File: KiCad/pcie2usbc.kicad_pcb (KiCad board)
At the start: 4 copper layers, 35.3 x 24 mm, 126 parts, among them J2 USB-C-MLX, J3 Bus_PCI_Express_x4, J4 Conn_02x05_Top_Bottom, J5 USB-C-MLX

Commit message: WiP layout
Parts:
- removed the C1 at (194.6, 94.7)
- removed the C10 at (194.6, 97.5)
- removed the C10 at (145.9, 97.8)
- removed the C11 at (194.6, 100.3)
- removed the C11 at (145.9, 96.0)
- removed the C12 at (194.6, 103.1)
- removed the C12 at (145.9, 103.0)
- removed the C13 at (194.6, 105.9)
- removed the C13 at (145.9, 101.3)
- removed the C16 at (223.7, 94.7)
- removed the C16 at (159.2, 104.0)
- removed the C17 at (223.0, 108.3)
- removed the C17 at (160.2, 104.0)
- removed the C2 at (158.2, 104.0)
- removed the C3 at (162.4, 104.0)
- removed the C4 at (193.9, 112.5)
- removed the C4 at (161.4, 104.0)
- removed the C5 at (193.9, 114.6)
- removed the C5 at (156.9, 104.0)
- removed the C6 at (193.9, 116.7)
- removed the C6 at (157.9, 104.0)
- removed the C7 at (162.2, 104.0)
- removed the C8 at (161.2, 104.0)
- removed the C9 at (196.9, 112.5)
- removed the C9 at (151.9, 96.0)
- removed the J2 at (185.4, 98.5)
- removed the R10 at (199.8, 77.9)
- removed the R10 at (145.9, 99.5)
- removed the R2 at (198.9, 97.5)
- removed the R2 at (136.9, 106.5)
- removed R21: 0, pcie2usbc:R0603
- removed R22: 100k, pcie2usbc:R0603
- removed the R3 at (198.9, 100.3)
- removed the R3 at (151.9, 103.0)
- removed the R4 at (198.9, 103.1)
- removed the R4 at (151.9, 97.8)
- removed the R5 at (198.9, 105.9)
- removed the R5 at (151.9, 101.3)
- removed the R6 at (203.3, 94.7)
- removed the R6 at (151.9, 99.5)
- removed the R7 at (203.3, 97.5)
- removed the R7 at (134.7, 106.5)
- removed the R8 at (203.3, 100.3)
- removed the R8 at (132.4, 106.5)
- removed RST0, UNK12V0, UNK3V3: , pcie2usbc:SML0805
- removed TP1, TP2, TP21, TP3, TP4, TP5, TP6, TP7, TP8, TP9: TPB0,635, pcie2usbc:B0,635
- removed the TP13 at (180.7, 113.6)
- removed the TP13 at (164.7, 105.8)
- removed the TP16 at (159.7, 95.0)
- removed the TP16 at (187.6, 78.5)
- removed the TP19 at (191.6, 78.5)
- removed TP20, TP21, TP22, TP23, TP24, TP31, TP32, TP33, TP34, TP35, TP36, TP37, TP38: TestPoint, TestPoint:TestPoint_Pad_D2.0mm
- removed TP30: TPTP38X20, pcie2usbc:TP38X20
- removed UNK12V1, UNK12V2, UNK3V1, UNK3V2: LEDSML0805, pcie2usbc:SML0805
- added +12V1: LEDSML0805, pcie2usbc:SML0805, F.Cu at (149.2, 79.5)
- added +12V2: LEDSML0805, pcie2usbc:SML0805, F.Cu at (184.4, 78.9)
- added +3V1: LEDSML0805, pcie2usbc:SML0805, F.Cu at (146.6, 79.5)
- added +3V2: LEDSML0805, pcie2usbc:SML0805, F.Cu at (187.0, 78.7)
- added C10: 100n, pcie2usbc:C0402, B.Cu at (161.6, 89.9)
- added C11: 100n, pcie2usbc:C0402, B.Cu at (158.3, 86.0)
- added C12: 1u, pcie2usbc:C0603K, F.Cu at (145.3, 104.0)
- added C13: 100n, pcie2usbc:C0603K, F.Cu at (147.2, 104.0)
- added C16: 100n, pcie2usbc:C0603K, F.Cu at (169.0, 78.7)
- added C17: 100n, pcie2usbc:C0402, F.Cu at (180.9, 90.9)
- added C4: 100n, pcie2usbc:C0402, B.Cu at (153.3, 90.0)
- added C5: 100n, pcie2usbc:C0402, B.Cu at (160.2, 89.8)
- added C6: 100n, pcie2usbc:C0402, B.Cu at (157.1, 86.0)
- added C9: 100n, pcie2usbc:C0402, B.Cu at (154.6, 90.0)
- added R10: 0, Resistor_SMD:R_0402_1005Metric_Pad0.72x0.64mm_HandSolder, B.Cu at (145.3, 87.1)
- added R2: 0, Resistor_SMD:R_0402_1005Metric_Pad0.72x0.64mm_HandSolder, B.Cu at (172.2, 98.4)
- added R3: 2.2k, Resistor_SMD:R_0402_1005Metric_Pad0.72x0.64mm_HandSolder, F.Cu at (143.6, 83.1)
- added R4: 10k, Resistor_SMD:R_0402_1005Metric_Pad0.72x0.64mm_HandSolder, F.Cu at (149.1, 82.9)
- added R5: 2.2k, Resistor_SMD:R_0402_1005Metric_Pad0.72x0.64mm_HandSolder, F.Cu at (146.5, 83.0)
- added R7: 0, Resistor_SMD:R_0402_1005Metric_Pad0.72x0.64mm_HandSolder, B.Cu at (148.4, 87.1)
- added R8: 0, Resistor_SMD:R_0402_1005Metric_Pad0.72x0.64mm_HandSolder, B.Cu at (148.5, 86.0)
- added TP13: TestPoint, TestPoint:TestPoint_Pad_1.0x1.0mm, B.Cu at (141.7, 88.3)
- added TP15: TestPoint, TestPoint:TestPoint_Pad_1.0x1.0mm, F.Cu at (136.8, 87.3)
- added TP16: TestPoint, TestPoint:TestPoint_Pad_1.0x1.0mm, F.Cu at (137.0, 80.9)
- C1: footprint pcie2usbc:C0402 -> pcie2usbc:C0603K; moved to B.Cu
- C14: value 100n -> 1u; footprint pcie2usbc:C0402 -> pcie2usbc:C0603K
- C15: footprint pcie2usbc:C0402 -> pcie2usbc:C0603K
- C2, C27, C28, C29, C3, C30, C7, C8: moved to B.Cu
- J3: renamed from J2; footprint pcie2usbc:MOLEX_105450-0101 -> Connector_USB:USB_C_Receptacle_CNCTech_C-ARA1-AK51X
- J4: renamed from J5; footprint pcie2usbc:MOLEX_105450-0101 -> Connector_USB:USB_C_Receptacle_CNCTech_C-ARA1-AK51X
- R1: footprint pcie2usbc:R0603 -> Resistor_SMD:R_0402_1005Metric_Pad0.72x0.64mm_HandSolder; moved to B.Cu
- R11, R20: value 0 -> 100k; footprint pcie2usbc:R0603 -> Resistor_SMD:R_0402_1005Metric_Pad0.72x0.64mm_HandSolder
- R12: value 0 -> 2.2k; footprint pcie2usbc:R0603 -> Resistor_SMD:R_0402_1005Metric_Pad0.72x0.64mm_HandSolder
- R13: value 2.2k -> 10k; footprint pcie2usbc:R0603 -> Resistor_SMD:R_0402_1005Metric_Pad0.72x0.64mm_HandSolder
- R14: value 10k -> 2.2k; footprint pcie2usbc:R0603 -> Resistor_SMD:R_0402_1005Metric_Pad0.72x0.64mm_HandSolder
- R15: value 2.2k -> 0; footprint pcie2usbc:R0603 -> Resistor_SMD:R_0402_1005Metric_Pad0.72x0.64mm_HandSolder; moved to B.Cu
- R16: footprint pcie2usbc:R0603 -> Resistor_SMD:R_0402_1005Metric_Pad0.72x0.64mm_HandSolder; moved to F.Cu
- R17, R18, R19: footprint pcie2usbc:R0603 -> Resistor_SMD:R_0402_1005Metric_Pad0.72x0.64mm_HandSolder
- R6: renamed from R1; value 100k -> 0; footprint pcie2usbc:R0603 -> Resistor_SMD:R_0402_1005Metric_Pad0.72x0.64mm_HandSolder
- R9: value 100k -> 0; footprint pcie2usbc:R0603 -> Resistor_SMD:R_0402_1005Metric_Pad0.72x0.64mm_HandSolder; moved to B.Cu
- TP10: value TPTP38X20 -> TestPoint; footprint pcie2usbc:TP38X20 -> TestPoint:TestPoint_Pad_1.0x1.0mm
- TP11, TP12: value TPB0,635 -> TestPoint; footprint pcie2usbc:B0,635 -> TestPoint:TestPoint_Pad_1.0x1.0mm; moved to B.Cu
- TP14: renamed from TP10; footprint pcie2usbc:TP38X20 -> TestPoint:TestPoint_Pad_D1.5mm
- TP17, TP18: footprint TestPoint:TestPoint_Pad_D2.0mm -> TestPoint:TestPoint_Pad_1.0x1.0mm
- TP19: renamed from TP29; footprint pcie2usbc:TP38X20 -> TestPoint:TestPoint_Pad_D1.5mm
- moved C30 88.6 mm to (135.2, 102.3), turned to 180 degrees
- moved C29 88.5 mm to (135.2, 104.3), turned to 180 degrees
- moved R15 84.9 mm to (143.6, 91.5)
- moved C27 78.7 mm to (145.3, 104.0), turned to 90 degrees
- moved C28 76.6 mm to (147.2, 104.0), turned to 90 degrees
- moved R20 66.1 mm to (169.5, 77.1)
- moved C26 65.1 mm to (165.9, 91.9), turned to -90 degrees
- moved RST1 64.3 mm to (143.7, 79.5), turned to 90 degrees
- moved C21 63.6 mm to (164.5, 91.8), turned to -90 degrees
- moved C15 63.4 mm to (135.2, 102.3), turned to 180 degrees
- moved C14 62.6 mm to (135.2, 104.2), turned to 180 degrees
- moved R9 60.4 mm to (145.3, 86.0), turned to 180 degrees
- moved C25 59.3 mm to (171.3, 92.0), turned to -90 degrees
- moved R17 58.6 mm to (171.7, 86.8)
- moved C20 57.6 mm to (170.1, 92.0), turned to -90 degrees
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- renumbered J3 to J1, J4 to J2
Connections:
- C1 pad 1: RX1_P -> Net-(C1-Pad1)
- C1 pad 2: PER0_P -> GND
- C14 pad 1: /USB-C Lane1+2/TX2_N -> +3V3
- C14 pad 2: /PET1_N -> GND
- C15 pad 1: /USB-C Lane1+2/D_N -> +3V3
- C15 pad 2: /REFCLK_N -> GND
- J3 pad A10: RX2_N -> /USB-C Lane1+2/RX2_N
- J3 pad A11: RX2_P -> /USB-C Lane1+2/RX2_P
- J3 pad A2: TX1_P -> /USB-C Lane1+2/TX1_P
- J3 pad A3: TX1_N -> /USB-C Lane1+2/TX1_N
- J3 pad A4: VBUS -> /USB-C Lane1+2/VBUS
- J3 pad A5: CC1 -> /USB-C Lane1+2/CC1
- J3 pad A6: D_P -> /USB-C Lane1+2/D_P
- J3 pad A7: D_N -> /USB-C Lane1+2/D_N
- J3 pad A8: SBU1 -> /USB-C Lane1+2/SBU1
- J3 pad A9: VBUS -> /USB-C Lane1+2/VBUS
- J3 pad B10: RX1_N -> /USB-C Lane1+2/RX1_N
- J3 pad B11: RX1_P -> /USB-C Lane1+2/RX1_P
- J3 pad B2: TX2_P -> /USB-C Lane1+2/TX2_P
- J3 pad B3: TX2_N -> /USB-C Lane1+2/TX2_N
- J3 pad B4: VBUS -> /USB-C Lane1+2/VBUS
- J3 pad B5: CC2 -> /USB-C Lane1+2/CC2
- J3 pad B6: D_P -> /USB-C Lane1+2/D_P
- J3 pad B7: D_N -> /USB-C Lane1+2/D_N
- J3 pad B8: SBU2 -> /USB-C Lane1+2/SBU2
- J3 pad B9: VBUS -> /USB-C Lane1+2/VBUS
- J3 pad S1: USB_SHLD1 -> Net-(C1-Pad1)
- R1 pad 1: /VBUS_H -> /PRSNT_SEL
- R1 pad 2: /USB-C Lane1+2/VBUS -> /PRSNT2
- R11 pad 1: PRSNT_SEL -> GND
- R11 pad 2: PRSNT2_N -> Net-(C1-Pad1)
- R12 pad 1: /PRSNT1 -> /PERST_N
- R12 pad 2: /PRSNT_SEL -> Net-(R12-Pad2)
- R13 pad 1: /PERST_N -> GND
- R13 pad 2: Net-(R13-Pad2) -> Net-(+12V2-PadC)
- R15 pad 1: GND -> /VBUS_H
- R15 pad 2: Net-(R15-Pad2) -> /USB-C Lane3+4/VBUS
- R16 pad 1: PRSNT1_N -> /PRSNT2_N
- R16 pad 2: PRSNT_SEL -> /USB-C Lane3+4/SBU1
- R17 pad 1: /VBUS_H -> /PRSNT1_N
- R17 pad 2: /USB-C Lane3+4/VBUS -> /USB-C Lane3+4/SBU2
- R18 pad 1: /PRSNT2_N -> /PERST_N
- R18 pad 2: /USB-C Lane3+4/SBU1 -> /USB-C Lane3+4/CC1
- R19 pad 1: /PRSNT1_N -> /USB-C Lane3+4/CC2
- R19 pad 2: /USB-C Lane3+4/SBU2 -> /PERST_N
- R20 pad 1: /PERST_N -> GND
- R20 pad 2: /USB-C Lane3+4/CC1 -> Net-(C16-Pad1)
- R6 pad 1: GND -> /VBUS_H
- R6 pad 2: USB_SHLD1 -> /USB-C Lane1+2/VBUS
- R9 pad 1: GND -> /PERST_N
- R9 pad 2: Net-(C1-Pad1) -> /USB-C Lane1+2/CC1
- RST2 pad C: Net-(R13-Pad2) -> Net-(R12-Pad2)
- TP17 pad 1: /SMDAT -> /USB-C Lane3+4/CC1
- TP18 pad 1: /TRST_N -> /USB-C Lane3+4/CC2
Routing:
- net +3V3: track 0.00 -> 129.3 mm, vias 0 -> 5
- net +12V: track 0.00 -> 128.2 mm, vias 0 -> 6
- net /PERST_N: track 0.00 -> 89.5 mm, vias 0 -> 4
- net /REFCLK_N: track 0.00 -> 69.5 mm, vias 0 -> 3
- net /SMDAT: track 0.00 -> 60.8 mm, vias 0 -> 1
- net /TDO: track 0.00 -> 57.3 mm, vias 0 -> 1
- net /TDI: track 0.00 -> 56.9 mm, vias 0 -> 1
- net /VBUS_H: track 0.00 -> 55.0 mm, vias 0 -> 3
- net /TRST_N: track 0.00 -> 52.6 mm, vias 0 -> 1
- net /TMS: track 0.00 -> 52.5 mm, vias 0 -> 2
- net 12V0: track 51.7 -> 0.00 mm, vias 5 -> 0
- net /USB-C Lane3+4/VBUS: track 0.00 -> 47.6 mm
- net /WAKE_N: track 0.00 -> 46.9 mm, vias 0 -> 1
- net /USB-C Lane1+2/SBU2: track 0.00 -> 44.0 mm, vias 0 -> 2
- net 3V3: track 44.0 -> 0.00 mm, vias 6 -> 0
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- removed copper zone on F.Cu, net GND
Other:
- board size 35.3 x 24 mm -> 83.1 x 37.3 mm

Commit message: routing completed - review requested
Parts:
- TP15: moved to B.Cu
- moved TP15 30.3 mm to (167.1, 84.5), turned to 180 degrees
- moved TP16 29.4 mm to (166.0, 85.2)
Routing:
- net /TCK: track 13.5 -> 62.6 mm, vias 0 -> 3
- net GND: track 39.1 -> 87.8 mm, vias 13 -> 28
- net /SMCLK: track 19.4 -> 63.5 mm, vias 1 -> 2
- net /PRSNT2: track 14.8 -> 35.3 mm, vias 1 -> 3
- net /USB-C Lane3+4/SBU2: track 28.6 -> 48.9 mm, vias 1 -> 2
- net /USB-C Lane1+2/D_N: track 3.13 -> 9.99 mm, vias 0 -> 1
- net +3V3: track 129.3 -> 136.0 mm, vias 5 -> 6
- net /WAKE_N: track 46.9 -> 53.6 mm
- net +12V: track 128.2 -> 134.1 mm
- net Net-(C16-Pad1): track 27.8 -> 33.1 mm, vias 0 -> 1
- net /CLKREQ_N: track 41.5 -> 45.6 mm
- net /USB-C Lane3+4/SBU1: track 14.3 -> 18.0 mm
- net /USB-C Lane3+4/VBUS: track 47.6 -> 51.1 mm
- net /USB-C Lane1+2/VBUS: track 19.3 -> 22.3 mm
- net /USB-C Lane3+4/TX2_N: track 19.1 -> 19.9 mm
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- added copper zone on F.Cu, net GND
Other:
- board size 83.1 x 37.3 mm -> 64.5 x 37.3 mm

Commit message: v1.0 final for reviwe
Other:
- outline, holes or cut-outs redrawn
- board text added: "PCIe to USB-C x4 v1.0 2023.09"
- board text removed: "PCIe to USB-C v1A 2021.05"
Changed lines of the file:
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@@
   (gr_arc (start 176.850001 108.5) (mid 177.172157 107.743805) (end 177.963403 107.521217)
     (stroke (width 0.05) (type solid)) (layer "Edge.Cuts"))
-  (gr_arc (start 194.3249 75.2064) (mid 195.010645 75.497848) (end 195.293678 76.187109)
+  (gr_arc (start 194.3249 75.206395) (mid 195.010648 75.497844) (end 195.293678 76.187109)
     (stroke (width 0.05) (type solid)) (layer "Edge.Cuts"))
   (gr_arc (start 140.7011 104.8036) (mid 141.973892 105.330808) (end 142.5011 106.6036)
     (stroke (width 0.05) (type solid)) (layer "Edge.Cuts"))
-  (gr_line (start 130.8511 111.5036) (end 130.85 76.23)
+  (gr_line (start 130.8511 111.5036) (end 130.828216 76.231936)
     (stroke (width 0.05) (type solid)) (layer "Edge.Cuts"))
   (gr_line (start 140.7011 104.8036) (end 140.6511 104.8036)
     (stroke (width 0.05) (type solid)) (layer "Edge.Cuts"))
-  (gr_arc (start 130.903566 76.224362) (mid 131.147083 75.508552) (end 131.85 75.230001)
+  (gr_arc (start 130.828216 76.231936) (mid 131.10208 75.489244) (end 131.85 75.230001)
     (stroke (width 0.05) (type default)) (layer "Edge.Cuts"))
   (gr_line (start 138.8511 106.6036) (end 138.8511 111.5036)
     (stroke (width 0.05) (type solid)) (layer "Edge.Cuts"))
-  (gr_arc (start 195.351107 106.422893) (mid 195.058216 107.130004) (end 194.351107 107.422893)
+  (gr_arc (start 195.351107 106.422893) (mid 195.058217 107.130007) (end 194.351107 107.422907)
     (stroke (width 0.05) (type solid)) (layer "Edge.Cuts"))
   (gr_arc (start 138.8511 111.5036) (mid 138.558207 112.210707) (end 137.8511 112.5036)
@@
   (gr_line (start 137.8511 112.5036) (end 131.8511 112.5036)
     (stroke (width 0.05) (type solid)) (layer "Edge.Cuts"))
-  (gr_text "PCIe to USB-C\nv1A 2021.05" (at 136.1511 95.2536 180) (layer "F.SilkS")
+  (gr_text "PCIe to USB-C x4\nv1.0 2023.09" (at 137.09 95.77 180) (layer "F.SilkS")
     (effects (font (size 0.666496 0.666496) (thickness 0.146304)))
   )

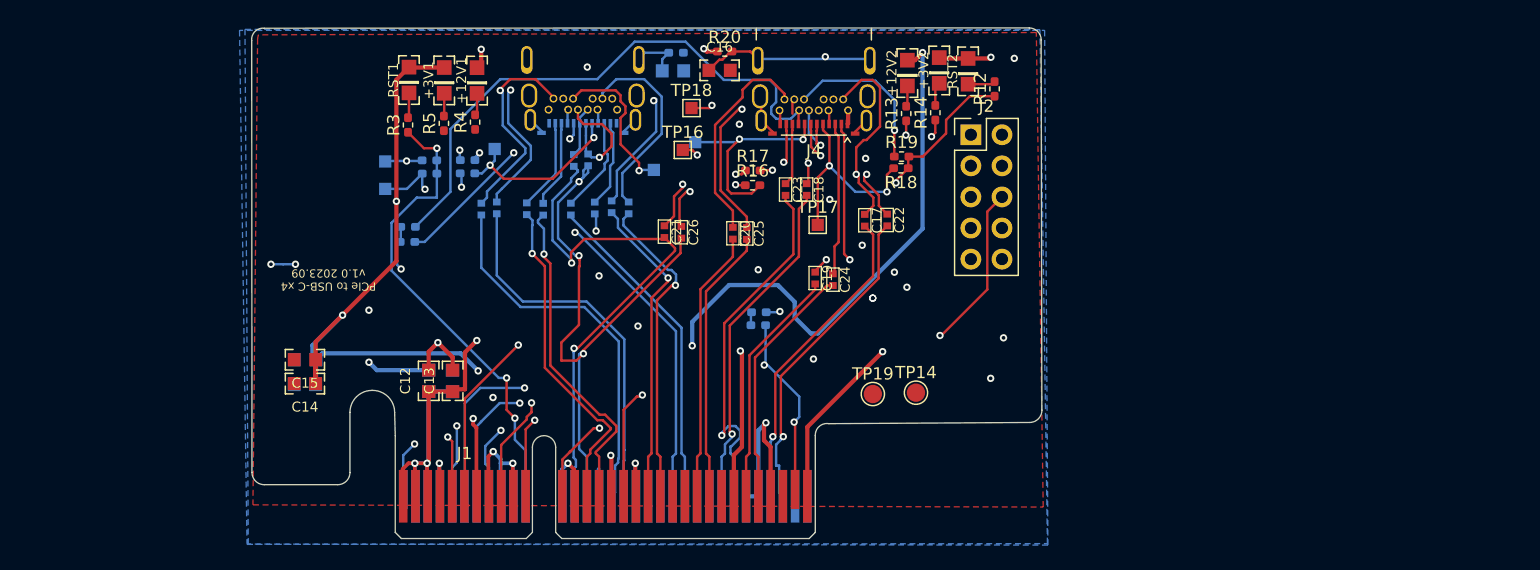
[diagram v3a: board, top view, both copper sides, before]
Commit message: reviwe - impedance matching
as the impedance network settings didn't apply correctly, layout was redone with correct impedance
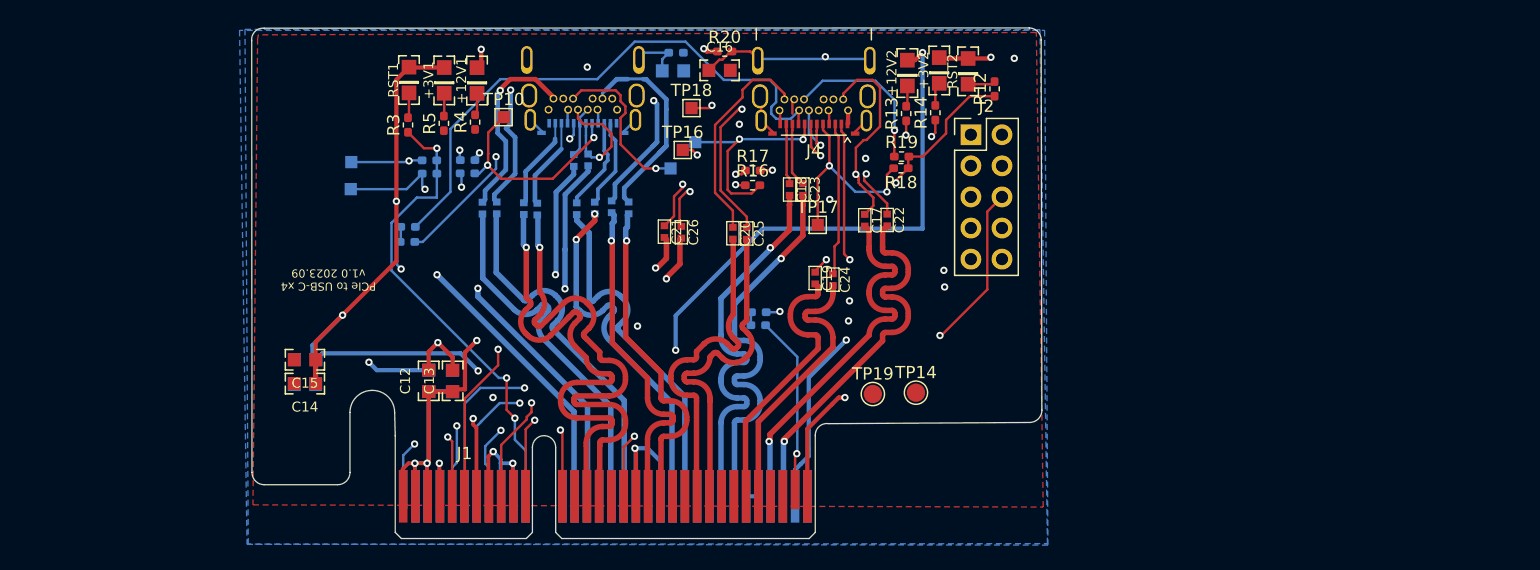
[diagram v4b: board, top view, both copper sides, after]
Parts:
- TP10: moved to F.Cu
- moved TP13 2.81 mm to (138.9, 88.4)
- moved TP12 2.77 mm to (139.0, 86.2)
- moved TP10 2.70 mm to (151.4, 82.5), turned to 0 degrees
- moved C23 1.42 mm to (175.8, 88.4)
- moved C18 1.40 mm to (174.8, 88.4)
- moved TP11 1.37 mm to (165.0, 86.7)
- moved C8 0.48 mm to (157.4, 90.0)
- moved C9 0.48 mm to (154.2, 90.0)
- moved C4 0.24 mm to (153.1, 90.0)
- moved C2 0.12 mm to (149.7, 89.9)
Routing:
- net GND: track 87.8 -> 69.3 mm, vias 28 -> 17
- net /REFCLK_N: track 69.5 -> 51.1 mm
- net /PET0_N: track 26.9 -> 41.0 mm
- net /PET0_P: track 26.9 -> 41.1 mm
- net /REFCLK_P: track 44.0 -> 53.3 mm, vias 2 -> 3
- net /PET2_P: track 22.2 -> 27.8 mm
- net /PER3_P: track 25.8 -> 31.1 mm
- net /PET2_N: track 22.5 -> 27.7 mm
- net /PER2_P: track 27.6 -> 32.5 mm
- net /PER3_N: track 26.4 -> 31.2 mm
- net +12V: track 134.1 -> 130.7 mm
- net /PET3_P: track 19.7 -> 22.9 mm
- net /USB-C Lane1+2/SBU1: track 14.6 -> 17.5 mm
- net /USB-C Lane1+2/CC2: track 24.7 -> 27.6 mm
- net /PER1_N: track 26.6 -> 29.4 mm
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
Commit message: Final rework
Layout completed finally
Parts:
- removed J4: USB-C-MLX, Connector_USB:USB_C_Receptacle_CNCTech_C-ARA1-AK51X
- removed R16, R17, R18, R19: 0, Resistor_SMD:R_0402_1005Metric_Pad0.72x0.64mm_HandSolder
- removed R20: 100k, Resistor_SMD:R_0402_1005Metric_Pad0.72x0.64mm_HandSolder
- added GND1: TestPoint, TestPoint:TestPoint_Keystone_5015_Micro-Minature, F.Cu at (190.7, 104.2)
- added JP3: 0, Resistor_SMD:R_0402_1005Metric_Pad0.72x0.64mm_HandSolder, B.Cu at (185.6, 80.3)
- added JP4: 0, Resistor_SMD:R_0402_1005Metric_Pad0.72x0.64mm_HandSolder, B.Cu at (188.1, 80.3)
- added JP5: 0, Resistor_SMD:R_0402_1005Metric_Pad0.72x0.64mm_HandSolder, B.Cu at (186.8, 80.3)
- added JP6: 0, Resistor_SMD:R_0402_1005Metric_Pad0.72x0.64mm_HandSolder, B.Cu at (187.8, 87.2)
- added JP7: 0, Resistor_SMD:R_0402_1005Metric_Pad0.72x0.64mm_HandSolder, B.Cu at (185.4, 87.1)
- added TP1: TestPoint_Small, TestPoint:TestPoint_Pad_D1.0mm, F.Cu at (148.4, 99.0)
- added TP2: TestPoint_Small, TestPoint:TestPoint_Pad_D1.0mm, B.Cu at (146.1, 99.0)
- added TP3: TestPoint_Small, TestPoint:TestPoint_Pad_D1.0mm, F.Cu at (146.0, 104.0)
- added TP4: TestPoint_Small, TestPoint:TestPoint_Pad_D1.0mm, B.Cu at (151.0, 98.9)
- added TP5: TestPoint_Small, TestPoint:TestPoint_Pad_D1.0mm, F.Cu at (151.3, 103.9)
- added TP6: TestPoint_Small, TestPoint:TestPoint_Pad_D1.0mm, B.Cu at (150.3, 101.8)
- added TP7: TestPoint_Small, TestPoint:TestPoint_Pad_D1.0mm, F.Cu at (153.2, 100.0)
- added TP8: TestPoint_Small, TestPoint:TestPoint_Pad_D1.0mm, F.Cu at (148.7, 103.9)
- added TP9: TestPoint_Small, TestPoint:TestPoint_Pad_D1.0mm, F.Cu at (154.5, 103.8)
- +12V2, +3V2, C20, C21, C22, C23, C24, C25, C26, RST2: moved to B.Cu
- C1: value 100n -> 1u; moved to F.Cu
- C10, C7, C8, C9: moved to F.Cu
- C12: value 1u -> 100n; footprint pcie2usbc:C0603K -> pcie2usbc:C0402; moved to B.Cu
- C13, C28: footprint pcie2usbc:C0603K -> pcie2usbc:C0402
- C14, C27, C29: value 1u -> 100n; footprint pcie2usbc:C0603K -> pcie2usbc:C0402
- C16: value 100n -> 1u
- C17, C19: footprint pcie2usbc:C0402 -> pcie2usbc:C0603K
- C18: value 100n -> 1u; footprint pcie2usbc:C0402 -> pcie2usbc:C0603K
- C2, C4: footprint pcie2usbc:C0402 -> pcie2usbc:C0603K; moved to F.Cu
- C3: value 100n -> 1u; footprint pcie2usbc:C0402 -> pcie2usbc:C0603K; moved to F.Cu
- J2: value Conn_02x05_Top_Bottom -> USB-C-MLX; footprint Connector_PinHeader_2.54mm:PinHeader_2x05_P2.54mm_Vertical -> Connector_USB:USB_C_Receptacle_Amphenol_12401610E4-2A
- J3: footprint Connector_USB:USB_C_Receptacle_CNCTech_C-ARA1-AK51X -> Connector_USB:USB_C_Receptacle_Amphenol_12401610E4-2A
- JP10: renamed from R12; value 2.2k -> 0
- JP11: renamed from R13; value 10k -> 0
- JP12: renamed from R14; value 2.2k -> 0
- JP8: renamed from R10; moved to F.Cu
- JP9: renamed from R11; value 100k -> 0; moved to F.Cu
- R4: renamed from R6; value 0 -> 100k
- R5: renamed from R7; value 0 -> 2.2k
- R6: renamed from R8; value 0 -> 10k
- R7: renamed from R9; value 0 -> 2.2k
- R8: renamed from R15; value 0 -> 100k
- TP10: value TestPoint -> TestPoint_Small; footprint TestPoint:TestPoint_Pad_1.0x1.0mm -> TestPoint:TestPoint_Pad_D1.0mm
- TP14: value TPTP38X20 -> TestPoint; footprint TestPoint:TestPoint_Pad_D1.5mm -> TestPoint:TestPoint_Pad_1.0x1.0mm; moved to B.Cu
- TP15: footprint TestPoint:TestPoint_Pad_1.0x1.0mm -> TestPoint:TestPoint_Keystone_5015_Micro-Minature
- TP19: value TPTP38X20 -> TestPoint; footprint TestPoint:TestPoint_Pad_D1.5mm -> TestPoint:TestPoint_Pad_1.0x1.0mm
- moved RST2 49.5 mm to (139.8, 79.0)
- moved TP13 49.0 mm to (187.8, 84.8), turned to -90 degrees
- moved TP12 47.5 mm to (185.7, 77.8), turned to -90 degrees
- moved +3V2 44.8 mm to (142.2, 79.0)
- moved C19 43.8 mm to (136.3, 79.0)
- moved C2 42.6 mm to (192.1, 94.2)
- moved +12V1 41.7 mm to (191.0, 80.1)
- moved R2 41.7 mm to (190.8, 83.5)
- moved RST1 41.7 mm to (185.4, 80.0)
- moved +3V1 41.7 mm to (188.3, 80.1)
- moved R1 41.7 mm to (185.3, 83.7)
- moved R3 41.7 mm to (188.2, 83.6)
- moved C18 41.5 mm to (134.3, 79.1)
- moved JP10 40.5 mm to (151.0, 80.3)
- moved +12V2 39.6 mm to (144.8, 79.2)
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- renumbered R1 to JP1, R2 to JP2, R3 to R1, R4 to R2, R5 to R3
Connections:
- C1 pad 1: Net-(C1-Pad1) -> +12V
- C10 pad 1: /USB-C Lane1+2/TX2_N -> /USB-C Lane1+2/TX1_N
- C10 pad 2: /PET1_N -> /PET0_N
- C11 pad 1: /USB-C Lane1+2/D_N -> /USB-C Lane1+2/TX2_P
- C11 pad 2: /REFCLK_N -> /PET1_P
- C12 pad 1: +12V -> /USB-C Lane1+2/TX2_N
- C12 pad 2: GND -> /PET1_N
- C13 pad 1: +12V -> /USB-C Lane1+2/D_P
- C13 pad 2: GND -> /REFCLK_P
- C14 pad 1: +3V3 -> /USB-C Lane1+2/D_N
- C14 pad 2: GND -> /REFCLK_N
- C15 pad 1: +3V3 -> Net-(J2-SHIELD)
- C16 pad 1: Net-(C16-Pad1) -> +12V
- C17 pad 1: /USB-C Lane3+4/RX1_P -> +12V
- C17 pad 2: /PER3_P -> GND
- C18 pad 1: /USB-C Lane3+4/RX2_P -> +3V3
- C18 pad 2: /PER2_P -> GND
- C19 pad 1: /USB-C Lane3+4/TX1_P -> +3V3
- C19 pad 2: /PET3_P -> GND
- C2 pad 1: /USB-C Lane1+2/RX1_P -> +12V
- C2 pad 2: /PER0_P -> GND
- C20 pad 1: /USB-C Lane3+4/TX2_P -> /USB-C Lane3+4/RX1_P
- C20 pad 2: /PET2_P -> /PER3_P
- C21 pad 1: /USB-C Lane3+4/D_P -> /USB-C Lane3+4/RX1_N
- C21 pad 2: /REFCLK_P -> /PER3_N
- C22 pad 1: /USB-C Lane3+4/RX1_N -> /USB-C Lane3+4/RX2_P
- C22 pad 2: /PER3_N -> /PER2_P
- C24 pad 1: /USB-C Lane3+4/TX1_N -> /USB-C Lane3+4/TX1_P
- C24 pad 2: /PET3_N -> /PET3_P
- C25 pad 1: /USB-C Lane3+4/TX2_N -> /USB-C Lane3+4/TX1_N
- C25 pad 2: /PET2_N -> /PET3_N
- C26 pad 1: /USB-C Lane3+4/D_N -> /USB-C Lane3+4/TX2_P
- C26 pad 2: /REFCLK_N -> /PET2_P
- C27 pad 1: +12V -> /USB-C Lane3+4/TX2_N
- C27 pad 2: GND -> /PET2_N
- C28 pad 1: +12V -> /USB-C Lane3+4/D_P
- C28 pad 2: GND -> /REFCLK_P
- C29 pad 1: +3V3 -> /USB-C Lane3+4/D_N
- C29 pad 2: GND -> /REFCLK_N
- C3 pad 1: /USB-C Lane1+2/RX2_P -> +3V3
- C3 pad 2: /PER1_P -> GND
- C30 pad 1: +3V3 -> Net-(J3-SHIELD)
- C4 pad 1: /USB-C Lane1+2/TX1_P -> +3V3
- C4 pad 2: /PET0_P -> GND
- C5 pad 1: /USB-C Lane1+2/TX2_P -> /USB-C Lane1+2/RX1_P
- C5 pad 2: /PET1_P -> /PER0_P
- C6 pad 1: /USB-C Lane1+2/D_P -> /USB-C Lane1+2/RX1_N
- C6 pad 2: /REFCLK_P -> /PER0_N
- C7 pad 1: /USB-C Lane1+2/RX1_N -> /USB-C Lane1+2/RX2_P
- C7 pad 2: /PER0_N -> /PER1_P
- C9 pad 1: /USB-C Lane1+2/TX1_N -> /USB-C Lane1+2/TX1_P
- C9 pad 2: /PET0_N -> /PET0_P
- J1 pad B17: /PRSNT2 -> unconnected-(J1-~{PRSNT2}-PadB17)
- J3 pad A10: /USB-C Lane1+2/RX2_N -> /USB-C Lane3+4/RX2_N
- J3 pad A11: /USB-C Lane1+2/RX2_P -> /USB-C Lane3+4/RX2_P
- J3 pad A2: /USB-C Lane1+2/TX1_P -> /USB-C Lane3+4/TX1_P
- J3 pad A3: /USB-C Lane1+2/TX1_N -> /USB-C Lane3+4/TX1_N
- J3 pad A4: /USB-C Lane1+2/VBUS -> /USB-C Lane3+4/VBUS
- J3 pad A5: /USB-C Lane1+2/CC1 -> /USB-C Lane3+4/CC1
- J3 pad A6: /USB-C Lane1+2/D_P -> /USB-C Lane3+4/D_P
- J3 pad A7: /USB-C Lane1+2/D_N -> /USB-C Lane3+4/D_N
- J3 pad A8: /USB-C Lane1+2/SBU1 -> /USB-C Lane3+4/SBU1
- J3 pad A9: /USB-C Lane1+2/VBUS -> /USB-C Lane3+4/VBUS
- J3 pad B10: /USB-C Lane1+2/RX1_N -> /USB-C Lane3+4/RX1_N
- J3 pad B11: /USB-C Lane1+2/RX1_P -> /USB-C Lane3+4/RX1_P
- J3 pad B2: /USB-C Lane1+2/TX2_P -> /USB-C Lane3+4/TX2_P
- J3 pad B3: /USB-C Lane1+2/TX2_N -> /USB-C Lane3+4/TX2_N
- J3 pad B4: /USB-C Lane1+2/VBUS -> /USB-C Lane3+4/VBUS
- J3 pad B5: /USB-C Lane1+2/CC2 -> /USB-C Lane3+4/CC2
- J3 pad B6: /USB-C Lane1+2/D_P -> /USB-C Lane3+4/D_P
- J3 pad B7: /USB-C Lane1+2/D_N -> /USB-C Lane3+4/D_N
- J3 pad B8: /USB-C Lane1+2/SBU2 -> /USB-C Lane3+4/SBU2
- J3 pad B9: /USB-C Lane1+2/VBUS -> /USB-C Lane3+4/VBUS
- J3 pad S1: Net-(C1-Pad1) -> Net-(J3-SHIELD)
- JP1 pad 1: /PRSNT_SEL -> /PRSNT1
- JP1 pad 2: /PRSNT2 -> /PRSNT_SEL
- JP10 pad 2: Net-(R12-Pad2) -> /USB-C Lane3+4/SBU2
- JP11 pad 1: GND -> /PERST_N
- JP11 pad 2: Net-(+12V2-PadC) -> /USB-C Lane3+4/CC1
- JP12 pad 1: GND -> /USB-C Lane3+4/CC2
- JP12 pad 2: Net-(+3V2-PadC) -> /PERST_N
- JP2 pad 1: /PRSNT1 -> /PRSNT_SEL
- JP2 pad 2: /PRSNT_SEL -> /PRSNT2
- JP8 pad 1: /USB-C Lane1+2/CC2 -> /PERST_N
- JP8 pad 2: /PERST_N -> /USB-C Lane3+4/VBUS
- JP9 pad 1: GND -> /PRSNT2_N
- JP9 pad 2: Net-(C1-Pad1) -> /USB-C Lane3+4/SBU1
- R4 pad 1: /VBUS_H -> GND
- R4 pad 2: /USB-C Lane1+2/VBUS -> Net-(J2-SHIELD)
- R5 pad 1: /PRSNT2_N -> /PERST_N
- R5 pad 2: /USB-C Lane1+2/SBU1 -> Net-(R5-Pad2)
- R6 pad 1: /PRSNT1_N -> GND
- R6 pad 2: /USB-C Lane1+2/SBU2 -> Net-(+12V2-PadC)
- R7 pad 1: /PERST_N -> GND
- R7 pad 2: /USB-C Lane1+2/CC1 -> Net-(+3V2-PadC)
- R8 pad 1: /VBUS_H -> GND
- R8 pad 2: /USB-C Lane3+4/VBUS -> Net-(J3-SHIELD)
- RST2 pad C: Net-(R12-Pad2) -> Net-(R5-Pad2)
- TP10 pad 1: /USB-C Lane1+2/SBU1 -> /PERST_N
- TP11 pad 1: /USB-C Lane1+2/SBU2 -> /PERST_N
- TP12 pad 1: /USB-C Lane1+2/CC1 -> /USB-C Lane1+2/SBU2
- TP13 pad 1: /USB-C Lane1+2/CC2 -> /USB-C Lane1+2/CC1
- TP14 pad 1: (no net) -> /USB-C Lane1+2/CC2
- TP15 pad 1: /USB-C Lane3+4/SBU1 -> GND
- TP16 pad 1: /USB-C Lane3+4/SBU2 -> /USB-C Lane3+4/SBU1
- TP17 pad 1: /USB-C Lane3+4/CC1 -> /USB-C Lane3+4/SBU2
- TP18 pad 1: /USB-C Lane3+4/CC2 -> /USB-C Lane3+4/CC1
- TP19 pad 1: (no net) -> /USB-C Lane3+4/CC2
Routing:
- net /PERST_N: track 89.5 -> 230.0 mm, vias 4 -> 9
- net /VBUS_H: track 55.2 -> 0.00 mm, vias 2 -> 0
- net /SMDAT: track 63.3 -> 10.4 mm, vias 1 -> 0
- net /TCK: track 63.4 -> 14.9 mm, vias 3 -> 0
- net /SMCLK: track 64.9 -> 17.2 mm, vias 2 -> 0
- net Net-(J3-SHIELD): track 0.00 -> 45.6 mm
- net /TDO: track 57.3 -> 12.2 mm, vias 1 -> 0
- net /TRST_N: track 52.6 -> 9.58 mm, vias 1 -> 0
- net /TMS: track 51.7 -> 10.4 mm, vias 2 -> 1
- net /TDI: track 57.0 -> 15.7 mm, vias 1 -> 0
- net GND: track 69.3 -> 109.9 mm, vias 17 -> 16
- net /WAKE_N: track 53.4 -> 13.4 mm, vias 1 -> 0
- net /USB-C Lane3+4/SBU2: track 48.8 -> 10.8 mm
- net /CLKREQ_N: track 46.8 -> 10.4 mm, vias 1 -> 0
- net Net-(C16-Pad1): track 33.1 -> 0.00 mm, vias 1 -> 0
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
